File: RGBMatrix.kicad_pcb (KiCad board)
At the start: 8 copper layers, 23.5 x 50 mm, 248 parts, among them Q17 PNP, Q18 PNP, Q19 PNP, Q20 PNP, Q21 PNP, Q22 PNP, Q23 PNP, Q24 PNP, Q25 PNP, Q26 PNP, Q27 PNP, Q28 PNP, Q29 PNP, Q30 PNP, Q31 PNP, Q32 PNP, U1 74LS596, U2 74LS596, U3 74LS596, U4 74LS596, U5 74LS596, U6 74LS596, U8 74LS596, U9 74LS596

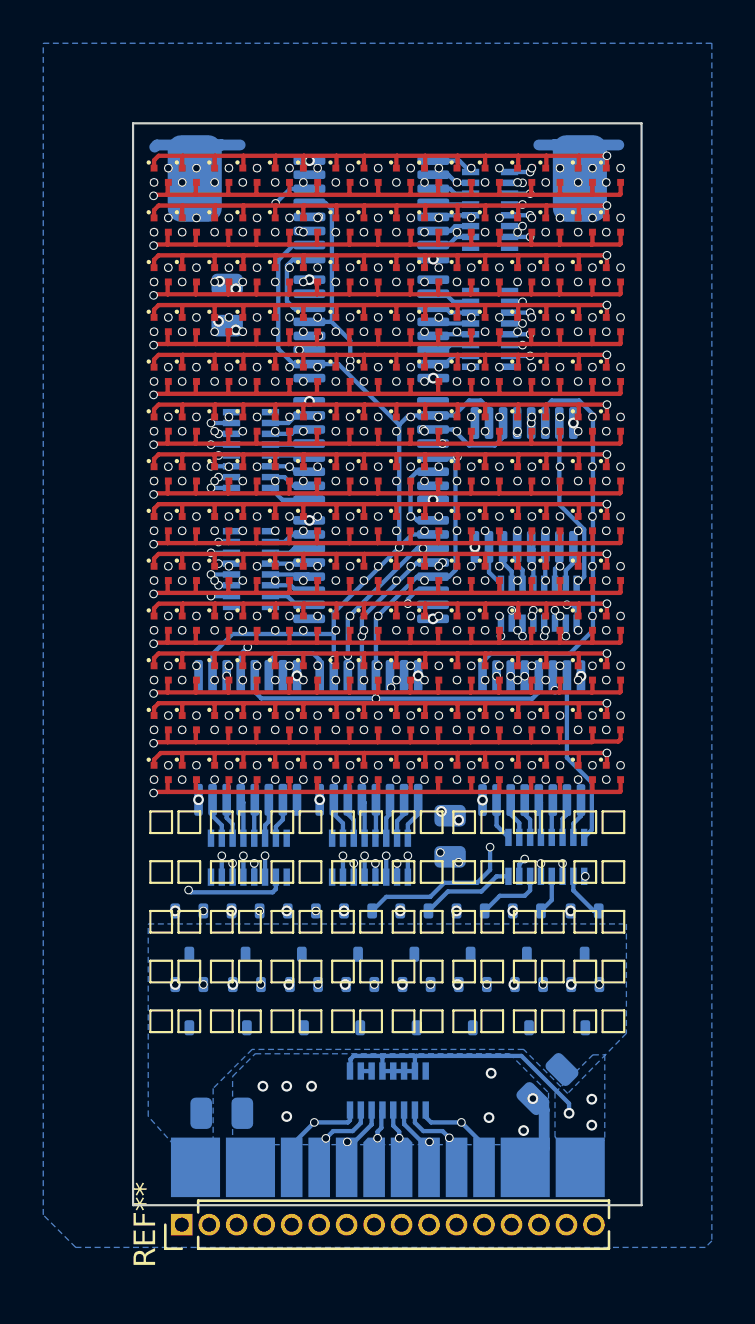
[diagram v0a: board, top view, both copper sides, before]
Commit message: High side switch, capacitors
replace fet-s with high side switches
added capacitors for every Shift Register power pin
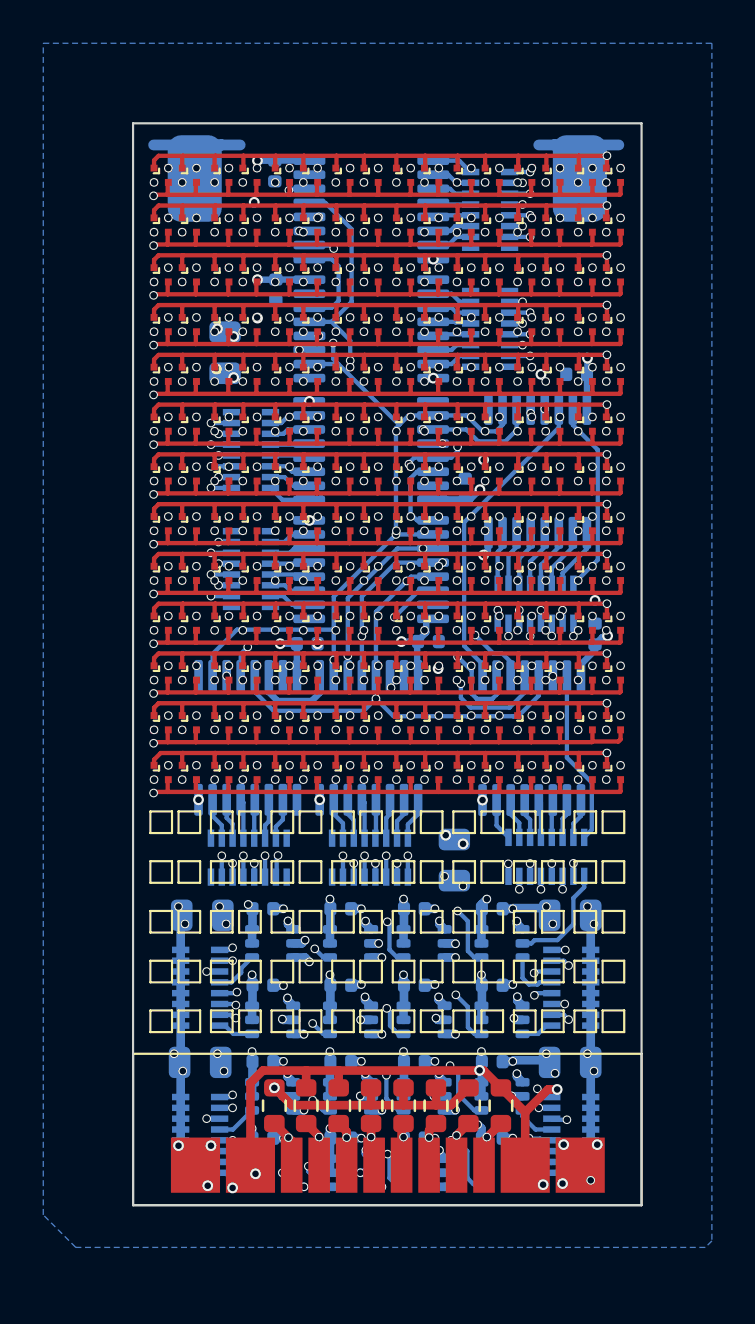
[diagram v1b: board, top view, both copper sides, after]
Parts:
- removed Q17, Q18, Q19, Q20, Q21, Q22, Q23, Q24, Q25, Q26, Q27, Q28, Q29, Q30, Q31, Q32: PNP, Package_TO_SOT_SMD:SOT-323_SC-70
- removed REF**: PinHeader_1x16_P1.27mm_Vertical, Connector_PinHeader_1.27mm:PinHeader_1x16_P1.27mm_Vertical
- removed RN9: R_Pack08, Resistor_SMD:R_Array_Convex_8x0602
- added C10: C, Capacitor_SMD:C_0402_1005Metric, B.Cu at (54.1, 89.4)
- added C11: C, Capacitor_SMD:C_0402_1005Metric, B.Cu at (54.1, 93.0)
- added C12: C, Capacitor_SMD:C_0402_1005Metric, B.Cu at (54.1, 96.5)
- added C13: C, Capacitor_SMD:C_0402_1005Metric, B.Cu at (50.7, 85.9)
- added C14: C, Capacitor_SMD:C_0402_1005Metric, B.Cu at (50.7, 89.4)
- added C15: C, Capacitor_SMD:C_0402_1005Metric, B.Cu at (50.7, 93.0)
- added C16: C, Capacitor_SMD:C_0402_1005Metric, B.Cu at (50.7, 96.5)
- added C17: C, Capacitor_SMD:C_0402_1005Metric, B.Cu at (47.1, 85.9)
- added C18: C, Capacitor_SMD:C_0402_1005Metric, B.Cu at (47.1, 89.4)
- added C19: C, Capacitor_SMD:C_0402_1005Metric, B.Cu at (47.1, 93.0)
- added C20: C, Capacitor_SMD:C_0402_1005Metric, B.Cu at (47.1, 96.5)
- added C21: C, Capacitor_SMD:C_0402_1005Metric, B.Cu at (62.5, 73.2)
- added C22: C, Capacitor_SMD:C_0402_1005Metric, B.Cu at (54.8, 73.5)
- added C23: C, Capacitor_SMD:C_0402_1005Metric, B.Cu at (61.6, 61.2)
- added C24: C, Capacitor_SMD:C_0402_1005Metric, B.Cu at (56.5, 66.5)
- added C25: C, Capacitor_SMD:C_0402_1005Metric, B.Cu at (47.6, 51.8)
- added C26: C, Capacitor_SMD:C_0402_1005Metric, B.Cu at (47.7, 57.3)
- added C27: C, Capacitor_SMD:C_0402_1005Metric, B.Cu at (49.1, 73.7)
- added C29: C, Capacitor_SMD:C_0805_2012Metric, B.Cu at (44.2, 93.0)
- added C30: C, Capacitor_SMD:C_0805_2012Metric, B.Cu at (44.3, 86.2)
- added C5: C, Capacitor_SMD:C_0402_1005Metric, B.Cu at (57.7, 85.9)
- added C6: C, Capacitor_SMD:C_0402_1005Metric, B.Cu at (57.7, 89.4)
- added C7: C, Capacitor_SMD:C_0402_1005Metric, B.Cu at (57.7, 93.0)
- added C8: C, Capacitor_SMD:C_0402_1005Metric, B.Cu at (57.7, 96.5)
- added C9: C, Capacitor_SMD:C_0402_1005Metric, B.Cu at (54.1, 85.9)
- added R1: R, Resistor_SMD:R_0603_1608Metric, F.Cu at (47.6, 95.0)
- added R2: R, Resistor_SMD:R_0603_1608Metric, F.Cu at (49.1, 95.0)
- added R3: R, Resistor_SMD:R_0603_1608Metric, F.Cu at (50.6, 95.0)
- added R4: R, Resistor_SMD:R_0603_1608Metric, F.Cu at (52.1, 95.0)
- added R5: R, Resistor_SMD:R_0603_1608Metric, F.Cu at (53.6, 95.0)
- added R6: R, Resistor_SMD:R_0603_1608Metric, F.Cu at (55.1, 95.0)
- added R7: R, Resistor_SMD:R_0603_1608Metric, F.Cu at (56.6, 95.0)
- added R8: R, Resistor_SMD:R_0603_1608Metric, F.Cu at (58.1, 95.0)
- added RN10: R_Pack08, Resistor_SMD:R_Array_Convex_8x0602, B.Cu at (61.4, 89.5)
- added RN11: R_Pack08, Resistor_SMD:R_Array_Convex_8x0602, B.Cu at (44.2, 89.5)
- added RN12: R_Pack08, Resistor_SMD:R_Array_Convex_8x0602, B.Cu at (61.4, 96.3)
- added RN13: R_Pack08, Resistor_SMD:R_Array_Convex_8x0602, B.Cu at (44.2, 96.3)
- added U10: FDG6323L-TP, FDG6323L:FDG6323L, B.Cu at (54.5, 94.6)
- added U11: FDG6323L-TP, FDG6323L:FDG6323L, B.Cu at (54.5, 91.0)
- added U12: FDG6323L-TP, FDG6323L:FDG6323L, B.Cu at (54.5, 87.5)
- added U13: FDG6323L-TP, FDG6323L:FDG6323L, B.Cu at (58.1, 98.1)
- added U14: FDG6323L-TP, FDG6323L:FDG6323L, B.Cu at (58.1, 94.6)
- added U15: FDG6323L-TP, FDG6323L:FDG6323L, B.Cu at (58.1, 91.0)
- added U16: FDG6323L-TP, FDG6323L:FDG6323L, B.Cu at (58.1, 87.5)
- added U17: FDG6323L-TP, FDG6323L:FDG6323L, B.Cu at (51.1, 87.5)
- added U18: FDG6323L-TP, FDG6323L:FDG6323L, B.Cu at (51.1, 91.0)
- added U19: FDG6323L-TP, FDG6323L:FDG6323L, B.Cu at (51.1, 94.6)
- added U20: FDG6323L-TP, FDG6323L:FDG6323L, B.Cu at (51.1, 98.1)
- added U21: FDG6323L-TP, FDG6323L:FDG6323L, B.Cu at (47.5, 87.5)
- added U22: FDG6323L-TP, FDG6323L:FDG6323L, B.Cu at (47.5, 91.0)
- added U23: FDG6323L-TP, FDG6323L:FDG6323L, B.Cu at (47.5, 94.6)
- added U24: FDG6323L-TP, FDG6323L:FDG6323L, B.Cu at (47.5, 98.1)
- added U7: FDG6323L-TP, FDG6323L:FDG6323L, B.Cu at (54.5, 98.1)
- moved C1 16.3 mm to (61.3, 93.0), turned to 180 degrees
- moved C2 7.87 mm to (61.3, 86.2), turned to 180 degrees
- moved C3 2.20 mm to (45.4, 60.2)
- moved C4 1.12 mm to (56.0, 83.7)
- moved U9 0.90 mm to (59.8, 65.7)
- moved RN8 0.15 mm to (59.7, 71.8)
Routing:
- net GND: track 22.6 -> 61.4 mm, vias 20 -> 49
- net G_IN: track 26.8 -> 48.4 mm, vias 2 -> 3
- net V_LED: track 0.00 -> 20.2 mm, vias 0 -> 28
- net +3.3V: track 18.9 -> 35.4 mm
- net COL13: track 1.81 -> 16.9 mm, vias 0 -> 2
- net COL09: track 4.36 -> 18.9 mm, vias 0 -> 2
- net Net-(RN11-R1.1): track 0.00 -> 14.5 mm, vias 0 -> 2
- net Net-(RN13-R1.1): track 0.00 -> 14.2 mm, vias 0 -> 2
- net Net-(RN10-R1.2): track 0.00 -> 14.2 mm, vias 0 -> 2
- net A13: track 34.7 -> 48.7 mm
- net Net-(RN13-R5.1): track 0.00 -> 13.7 mm, vias 0 -> 2
- net A01: track 34.5 -> 48.0 mm
- net A09: track 34.5 -> 48.1 mm
- net Net-(RN11-R5.1): track 0.00 -> 13.5 mm, vias 0 -> 2
- net Net-(RN12-R5.2): track 0.00 -> 12.9 mm, vias 0 -> 2
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- added copper zone on In2.Cu, net A01
- added copper zone on In2.Cu, net A02
- added copper zone on In2.Cu, net A03
- added copper zone on In2.Cu, net A04
- added copper zone on In2.Cu, net A05
- added copper zone on In2.Cu, net A06
- added copper zone on In2.Cu, net A07
- added copper zone on In2.Cu, net A08
- added copper zone on In2.Cu, net A09
- added copper zone on In2.Cu, net A10
- added copper zone on In2.Cu, net A11
- added copper zone on In2.Cu, net A12
- added copper zone on In2.Cu, net A13
- added copper zone on In2.Cu, net A14
- added copper zone on In2.Cu, net A15
- added copper zone on In2.Cu, net A16
- added copper zone on In5.Cu, net V_LED
- removed copper zone on B.Cu, net +3.3V
- removed copper zone on B.Cu, net V_LED

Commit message: separate anode control
removed control signals pull resistor, added "art", split control for anodes
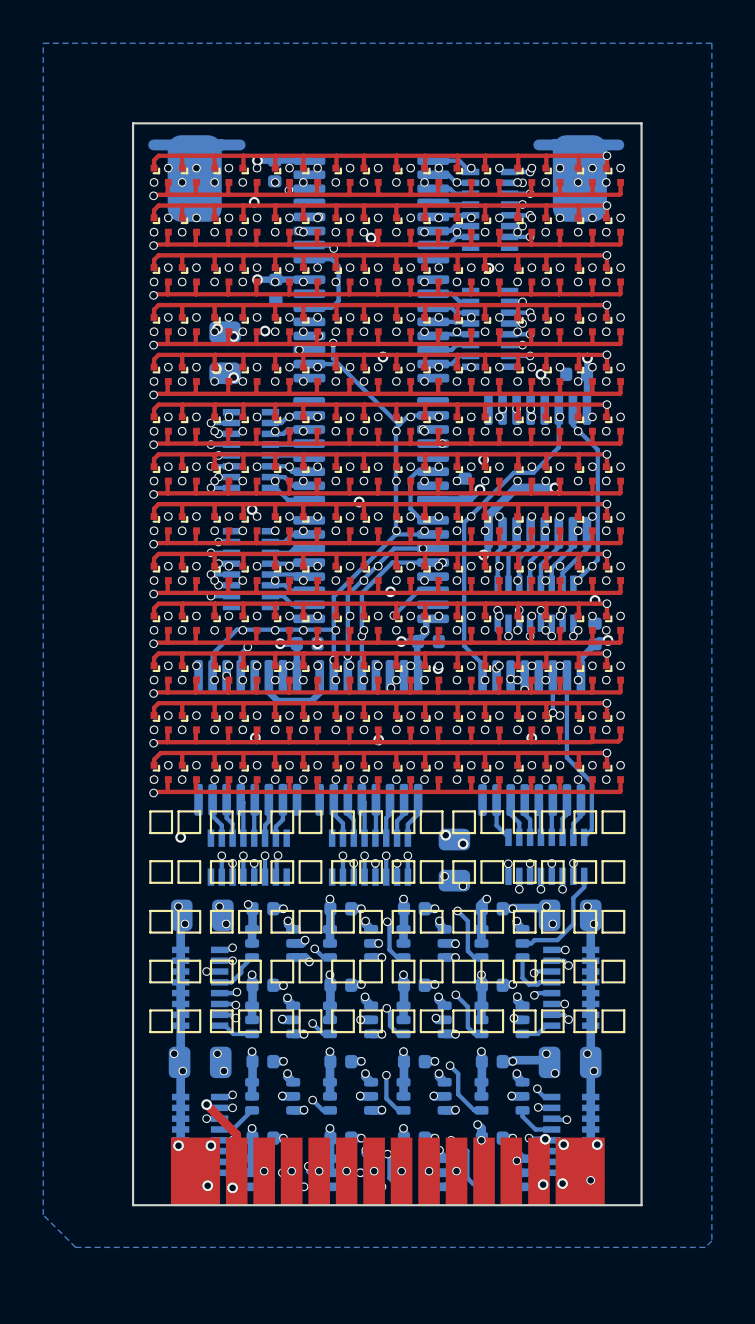
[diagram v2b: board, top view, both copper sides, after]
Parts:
- removed R1, R2, R3, R4, R5, R6, R7, R8: R, Resistor_SMD:R_0603_1608Metric
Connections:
- U1 pad 10: _SRCLR -> _SRCLR_RGB
- U1 pad 11: SRCLK -> SRCLK_RGB
- U1 pad 12: RCLK -> RCLK_RGB
- U1 pad 13: _EN -> GND
- U2 pad 10: _SRCLR -> _SRCLR_RGB
- U2 pad 11: SRCLK -> SRCLK_RGB
- U2 pad 12: RCLK -> RCLK_RGB
- U2 pad 13: _EN -> GND
- U3 pad 10: _SRCLR -> _SRCLR_RGB
- U3 pad 11: SRCLK -> SRCLK_RGB
- U3 pad 12: RCLK -> RCLK_RGB
- U3 pad 13: _EN -> GND
- U4 pad 10: _SRCLR -> _SRCLR_RGB
- U4 pad 11: SRCLK -> SRCLK_RGB
- U4 pad 12: RCLK -> RCLK_RGB
- U4 pad 13: _EN -> GND
- U5 pad 10: _SRCLR -> _SRCLR_RGB
- U5 pad 11: SRCLK -> SRCLK_RGB
- U5 pad 12: RCLK -> RCLK_RGB
- U5 pad 13: _EN -> GND
- U6 pad 10: _SRCLR -> _SRCLR_RGB
- U6 pad 11: SRCLK -> SRCLK_RGB
- U6 pad 12: RCLK -> RCLK_RGB
- U6 pad 13: _EN -> GND
- U8 pad 10: _SRCLR -> _SRCLR_A
- U8 pad 11: SRCLK -> SRCLK_A
- U8 pad 12: RCLK -> RCLK_A
- U8 pad 13: _EN -> GND
- U9 pad 10: _SRCLR -> _SRCLR_A
- U9 pad 11: SRCLK -> SRCLK_A
- U9 pad 12: RCLK -> RCLK_A
- U9 pad 13: _EN -> GND
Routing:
- net _EN: track 90.1 -> 0.00 mm, vias 8 -> 0
- net RCLK: track 90.0 -> 0.00 mm, vias 10 -> 0
- net _SRCLR: track 82.9 -> 0.00 mm, vias 7 -> 0
- net SRCLK: track 81.1 -> 0.00 mm, vias 9 -> 0
- net _SRCLR_RGB: track 0.00 -> 72.4 mm, vias 0 -> 5
- net RCLK_RGB: track 0.00 -> 71.0 mm, vias 0 -> 8
- net SRCLK_RGB: track 0.00 -> 65.1 mm, vias 0 -> 8
- net SRCLK_A: track 0.00 -> 45.3 mm, vias 0 -> 4
- net _SRCLR_A: track 0.00 -> 44.4 mm, vias 0 -> 4
- net RCLK_A: track 0.00 -> 43.5 mm, vias 0 -> 3
- net +3.3V: track 35.4 -> 18.1 mm, vias 15 -> 14
- net GND: track 61.4 -> 46.8 mm, vias 49 -> 52
- net G_IN: track 48.4 -> 43.3 mm
- net R_IN: track 47.6 -> 44.5 mm
- net Net-(RN12-R7.2): track 5.48 -> 7.17 mm
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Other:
- board text added: "Kifér az"
- board text added: "Lopják a"
- board text added: "Mátrixot"
- board text added: "Tedd vissza!"
- board text added: "VESZ- TETTEM"
- board text added: "You like looking at design files, don't you?"
- board text added: "ablakon"
- board text removed: "VESZTETTEM"

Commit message: update
design, values to resistors
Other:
- board text added: "Magic smoke extraction layer. If you see this, you lost your warranty 3 layers ago."

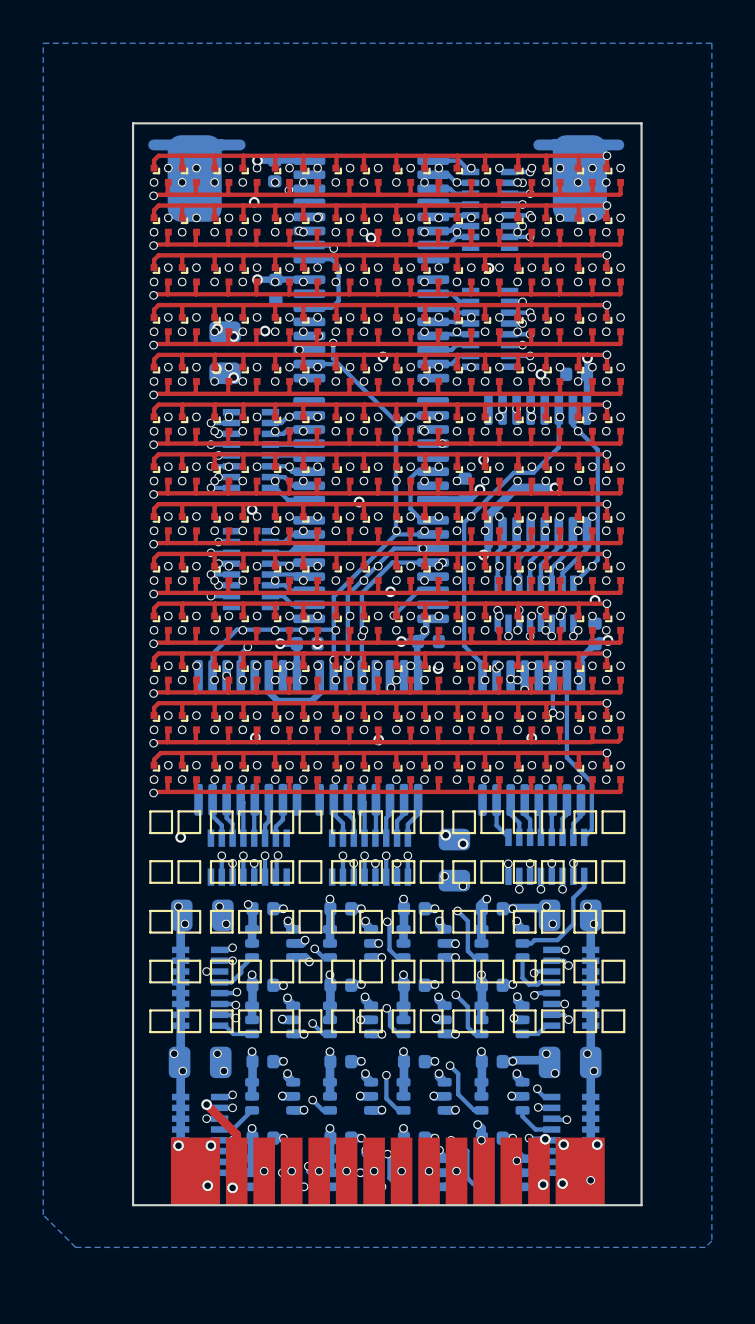
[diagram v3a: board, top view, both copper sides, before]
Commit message: updated filler zones
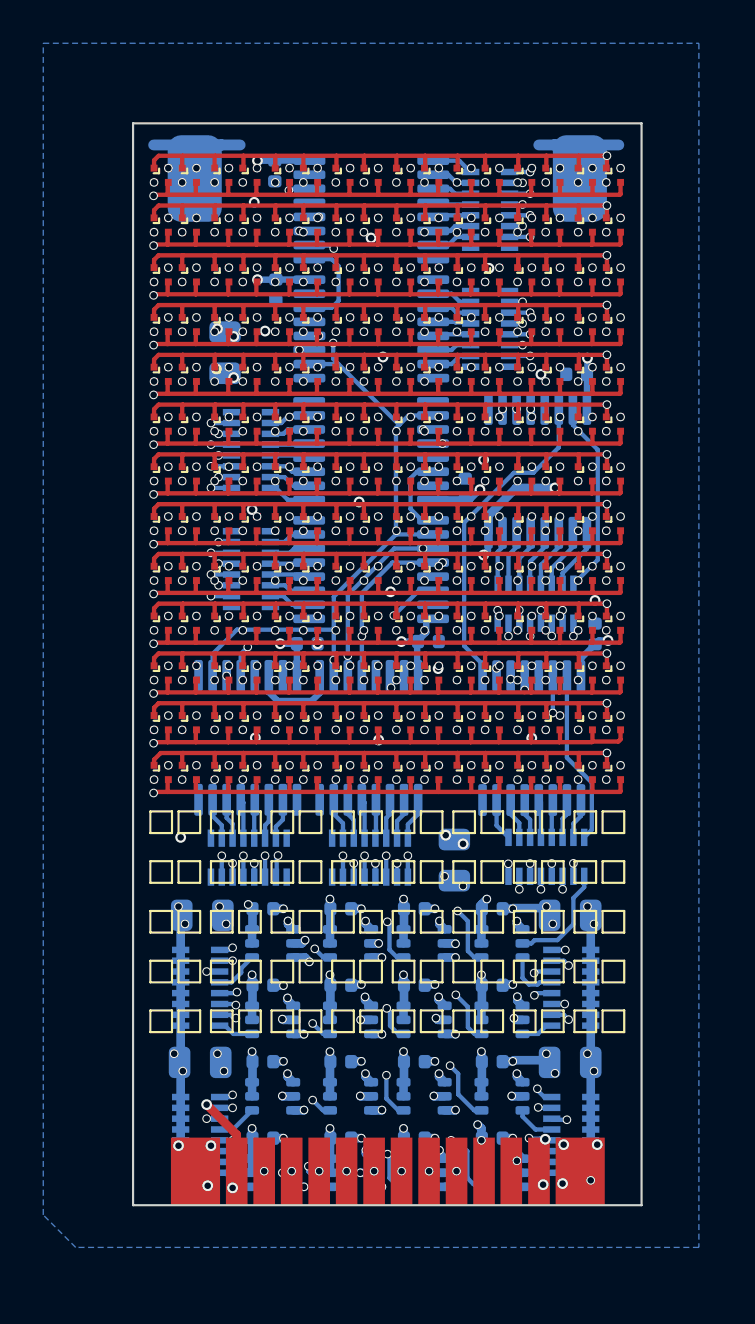
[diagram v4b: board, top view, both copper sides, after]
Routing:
- added copper zone on In1.Cu, net (none)
- added copper zone on In2.Cu, net (none)
- added copper zone on In3.Cu, net (none)
- added copper zone on In4.Cu, net (none)
- removed copper zone on In1.Cu, net GND
- removed copper zone on In2.Cu, net GND
- removed copper zone on In3.Cu, net GND
- removed copper zone on In4.Cu, net GND
